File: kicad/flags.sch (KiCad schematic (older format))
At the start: 3 parts, among them U48 74LS173

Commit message: Update to current kicad libraries
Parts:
- removed D68, D69: LED, symbol LED
- removed U48: 74LS173, symbol 74LS173
- added D62, D63: LED, symbol Device:LED
- added U48: 74LS173, symbol 74xx:74LS173
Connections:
- net labels added: VCC
- wire segments 27 -> 26
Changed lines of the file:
@@
-EESchema Schematic File Version 2
-LIBS:power
-LIBS:device
-LIBS:transistors
-LIBS:conn
-LIBS:linear
-LIBS:regul
-LIBS:74xx
-LIBS:cmos4000
-LIBS:adc-dac
-LIBS:memory
-LIBS:xilinx
-LIBS:microcontrollers
-LIBS:dsp
-LIBS:microchip
-LIBS:analog_switches
-LIBS:motorola
-LIBS:texas
-LIBS:intel
-LIBS:audio
-LIBS:interface
-LIBS:digital-audio
-LIBS:philips
-LIBS:display
-LIBS:cypress
-LIBS:siliconi
-LIBS:opto
-LIBS:atmel
-LIBS:contrib
-LIBS:valves
-LIBS:switches
-LIBS:74xxx
-LIBS:28c16
-LIBS:sap-be-cache
-EELAYER 24 0
+EESchema Schematic File Version 4
+EELAYER 30 0
 EELAYER END
 $Descr A4 11693 8268
 encoding utf-8
-Sheet 12 12
+Sheet 12 13
 Title "Simple As Possible computer by Ben Eater"
 Date "2017-05-10"
@@
 Text HLabel 4650 1600 2    60   Output ~ 0
 ZF
-$Comp
-L 74LS173 U48
-U 1 1 5AD47646
-P 3600 2050
-F 0 "U48" H 3700 2150 50  0000 C CNN
-F 1 "74LS173" H 3700 2000 50  0000 C CNN
-F 2 "" H 3600 2050 50  0000 C CNN
-F 3 "" H 3600 2050 50  0000 C CNN
-	1    3600 2050
-	1    0    0    -1
-$EndComp
 Text Label 1550 950  2    60   ~ 0
 ~LOAD
-Text Label 2550 2300 0    60   ~ 0
+Text Label 2950 2400 0    60   ~ 0
 ~LOAD
-$Comp
-L GND #PWR090
-U 1 1 5AD4767C
-P 2450 2100
-F 0 "#PWR090" H 2450 1850 50  0001 C CNN
-F 1 "GND" H 2450 1950 50  0000 C CNN
-F 2 "" H 2450 2100 50  0000 C CNN
-F 3 "" H 2450 2100 50  0000 C CNN
-	1    2450 2100
-	1    0    0    -1
-$EndComp
-Text Label 2550 1500 0    60   ~ 0
+Text Label 2950 1500 0    60   ~ 0
 CARRY
-Text Label 2550 1600 0    60   ~ 0
+Text Label 2950 1600 0    60   ~ 0
 ZERO
 Text Label 1550 1450 2    60   ~ 0
@@
 Text Label 1550 1250 2    60   ~ 0
 RST
-Text Label 2600 2600 0    60   ~ 0
+Text Label 3000 2700 0    60   ~ 0
 RST
 Wire Wire Line
 	1550 950  1300 950
 Wire Wire Line
-	2550 2300 2800 2300
+	2950 2400 3200 2400
 Wire Wire Line
-	2800 2300 2900 2300
+	3200 2400 3300 2400
 Wire Wire Line
-	2800 2300 2800 2200
+	3200 2400 3200 2300
 Wire Wire Line
-	2800 2200 2900 2200
-Connection ~ 2800 2300
+	3200 2300 3300 2300
+Connection ~ 3200 2400
 Wire Wire Line
-	2900 2050 2800 2050
+	3300 2100 3200 2100
 Wire Wire Line
-	2800 2050 2450 2050
+	3300 2000 3200 2000
 Wire Wire Line
-	2450 2050 2450 2100
+	3200 2000 3200 2100
+Connection ~ 3200 2100
 Wire Wire Line
-	2900 1950 2800 1950
+	2950 1500 3300 1500
 Wire Wire Line
-	2800 1950 2800 2050
-Connection ~ 2800 2050
-Wire Wire Line
-	2550 1500 2900 1500
-Wire Wire Line
-	2550 1600 2900 1600
+	2950 1600 3300 1600
 Wire Wire Line
 	1550 1450 1300 1450
@@
 	1550 1100 1300 1100
 Wire Wire Line
-	2550 2600 2900 2600
+	2950 2700 3300 2700
 Wire Wire Line
-	2550 2400 2900 2400
-Text Label 2550 2400 0    60   ~ 0
+	2950 2500 3300 2500
+Text Label 2950 2500 0    60   ~ 0
 CLK
 Text Label 4450 1500 0    60   ~ 0
@@
 NoConn ~ 4300 1700
 NoConn ~ 4300 1800
-NoConn ~ 2900 1700
-NoConn ~ 2900 1800
-$Comp
-L LED D68
-U 1 1 5AD4AD3C
-P 5450 1800
-F 0 "D68" H 5450 1900 50  0000 C CNN
-F 1 "LED" H 5450 1700 50  0000 C CNN
-F 2 "" H 5450 1800 50  0000 C CNN
-F 3 "" H 5450 1800 50  0000 C CNN
-	1    5450 1800
-	0    -1   -1   0
-$EndComp
-$Comp
-L LED D69
-U 1 1 5AD4AD4E
-P 5750 1800
-F 0 "D69" H 5750 1900 50  0000 C CNN
-F 1 "LED" H 5750 1700 50  0000 C CNN
-F 2 "" H 5750 1800 50  0000 C CNN
-F 3 "" H 5750 1800 50  0000 C CNN
-	1    5750 1800
-	0    -1   -1   0
-$EndComp
-$Comp
-L GND #PWR091
-U 1 1 5AD4AD59
-P 5600 2100
-F 0 "#PWR091" H 5600 1850 50  0001 C CNN
-F 1 "GND" H 5600 1950 50  0000 C CNN
-F 2 "" H 5600 2100 50  0000 C CNN
-F 3 "" H 5600 2100 50  0000 C CNN
-	1    5600 2100
-	1    0    0    -1
-$EndComp
+NoConn ~ 3300 1700
+NoConn ~ 3300 1800
 Wire Wire Line
 	5600 2100 5600 2050
@@
 Text Label 5750 1600 1    60   ~ 0
 ZF
+$Comp
+L power:GND #PWR0156
+U 1 1 5EA8388C
+P 2800 2100
+F 0 "#PWR0156" H 2800 1850 50  0001 C CNN
+F 1 "GND" H 2805 1927 50  0000 C CNN
+F 2 "" H 2800 2100 50  0001 C CNN
+F 3 "" H 2800 2100 50  0001 C CNN
+	1    2800 2100
+	1    0    0    -1
+$EndComp
+Wire Wire Line
+	2800 2100 3200 2100
+$Comp
+L power:GND #PWR0159
+U 1 1 5EA8545C
+P 5600 2100
+F 0 "#PWR0159" H 5600 1850 50  0001 C CNN
+F 1 "GND" H 5605 1927 50  0000 C CNN
+F 2 "" H 5600 2100 50  0001 C CNN
+F 3 "" H 5600 2100 50  0001 C CNN
+	1    5600 2100
+	1    0    0    -1
+$EndComp
+$Comp
+L Device:LED D62
+U 1 1 5EA85B93
+P 5450 1800
+F 0 "D62" V 5489 1683 50  0000 R CNN
+F 1 "LED" V 5398 1683 50  0000 R CNN
+F 2 "" H 5450 1800 50  0001 C CNN
+F 3 "~" H 5450 1800 50  0001 C CNN
+	1    5450 1800
+	0    -1   -1   0
+$EndComp
+$Comp
+L Device:LED D63
+U 1 1 5EA8646D
+P 5750 1800
+F 0 "D63" V 5789 1683 50  0000 R CNN
+F 1 "LED" V 5698 1683 50  0000 R CNN
+F 2 "" H 5750 1800 50  0001 C CNN
+F 3 "~" H 5750 1800 50  0001 C CNN
+	1    5750 1800
+	0    -1   -1   0
+$EndComp
+$Comp
+L 74xx:74LS173 U48
+U 1 1 5EA87D23
+P 3800 2100
+F 0 "U48" H 3550 2850 50  0000 C CNN
+F 1 "74LS173" H 4000 1350 50  0000 C CNN
+F 2 "" H 3800 2100 50  0001 C CNN
+F 3 "http://www.ti.com/lit/gpn/sn74LS173" H 3800 2100 50  0001 C CNN
+	1    3800 2100
+	1    0    0    -1
+$EndComp
+$Comp
+L power:GND #PWR0158
+U 1 1 5EA8EB64
+P 3800 3000
+F 0 "#PWR0158" H 3800 2750 50  0001 C CNN
+F 1 "GND" H 3805 2827 50  0000 C CNN
+F 2 "" H 3800 3000 50  0001 C CNN
+F 3 "" H 3800 3000 50  0001 C CNN
+	1    3800 3000
+	1    0    0    -1
+$EndComp
+$Comp
+L power:VCC #PWR0157
+U 1 1 5EA8F117
+P 3800 1200
+F 0 "#PWR0157" H 3800 1050 50  0001 C CNN
+F 1 "VCC" H 3817 1373 50  0000 C CNN
+F 2 "" H 3800 1200 50  0001 C CNN
+F 3 "" H 3800 1200 50  0001 C CNN
+	1    3800 1200
+	1    0    0    -1
+$EndComp
 $EndSCHEMATC

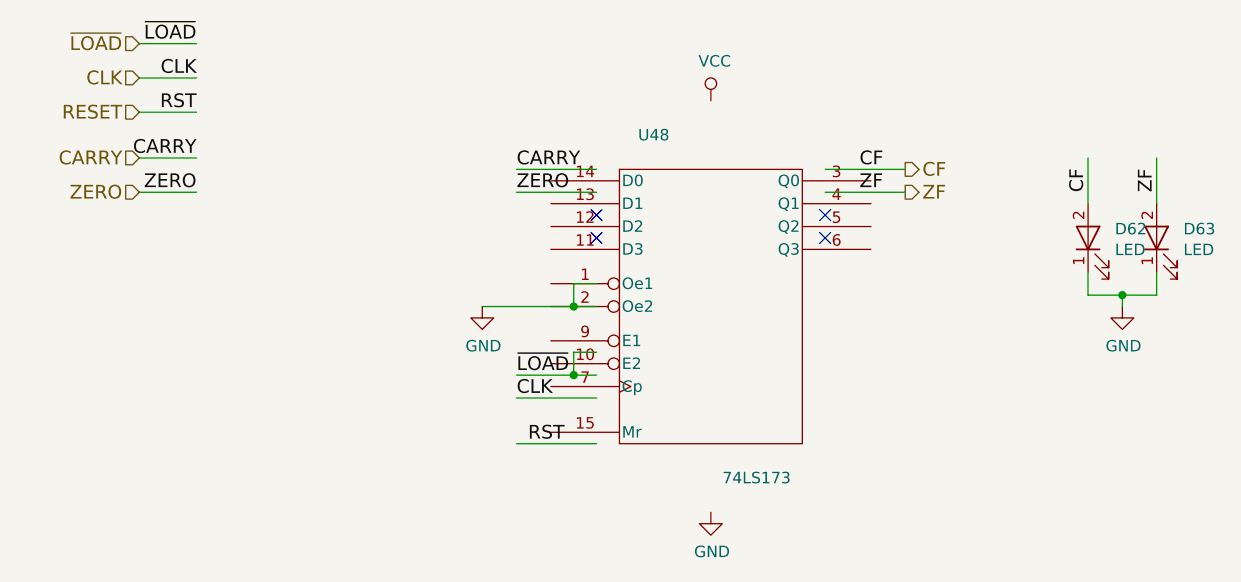
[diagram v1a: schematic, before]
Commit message: update bus names and improve sheet text
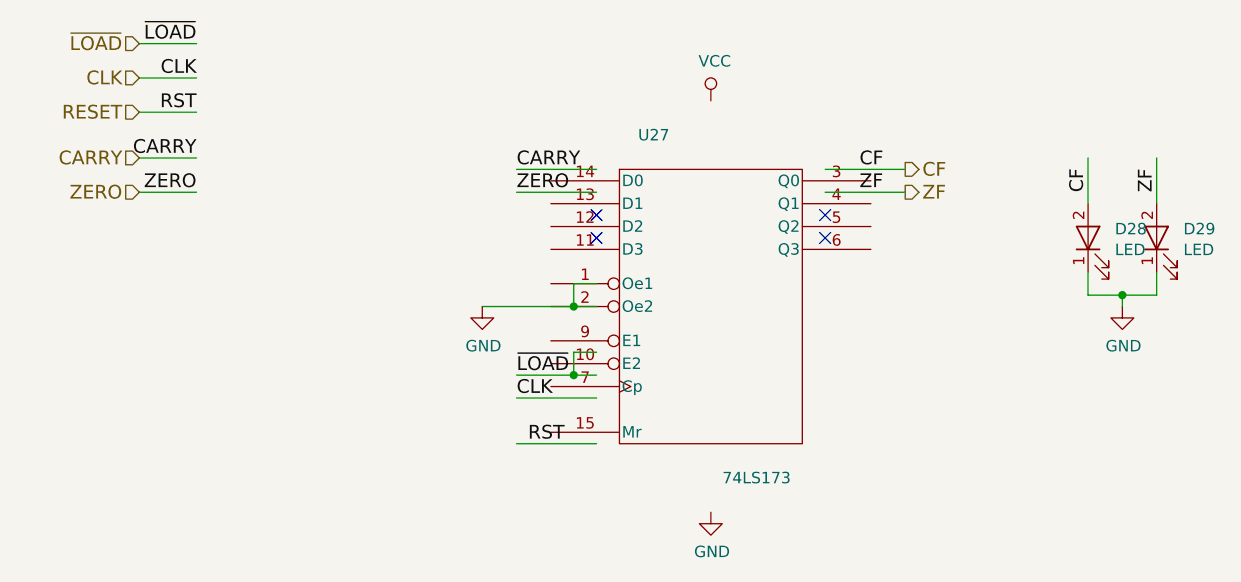
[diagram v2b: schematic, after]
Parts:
- renumbered D62 to D28, D63 to D29, U48 to U27
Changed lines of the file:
@@
 $Descr A4 11693 8268
 encoding utf-8
-Sheet 12 13
-Title "Simple As Possible computer by Ben Eater"
+Sheet 7 13
+Title "Simple As Possible computer"
 Date "2017-05-10"
 Rev "1"
 Comp "Schematic released as CC BY-SA"
-Comment1 "Schematic capture by Vincent Sanders"
+Comment1 "Schematic capture by Vincent Sanders of a design by Ben Eater"
 Comment2 "Flags register"
 Comment3 ""
@@
 ZF
 $Comp
-L power:GND #PWR0156
+L power:GND #PWR077
 U 1 1 5EA8388C
 P 2800 2100
-F 0 "#PWR0156" H 2800 1850 50  0001 C CNN
+F 0 "#PWR077" H 2800 1850 50  0001 C CNN
 F 1 "GND" H 2805 1927 50  0000 C CNN
 F 2 "" H 2800 2100 50  0001 C CNN
@@
 	2800 2100 3200 2100
 $Comp
-L power:GND #PWR0159
+L power:GND #PWR080
 U 1 1 5EA8545C
 P 5600 2100
-F 0 "#PWR0159" H 5600 1850 50  0001 C CNN
+F 0 "#PWR080" H 5600 1850 50  0001 C CNN
 F 1 "GND" H 5605 1927 50  0000 C CNN
 F 2 "" H 5600 2100 50  0001 C CNN
@@
 $EndComp
 $Comp
-L Device:LED D62
+L Device:LED D28
 U 1 1 5EA85B93
 P 5450 1800
-F 0 "D62" V 5489 1683 50  0000 R CNN
+F 0 "D28" V 5489 1683 50  0000 R CNN
 F 1 "LED" V 5398 1683 50  0000 R CNN
 F 2 "" H 5450 1800 50  0001 C CNN
@@
 $EndComp
 $Comp
-L Device:LED D63
+L Device:LED D29
 U 1 1 5EA8646D
 P 5750 1800
-F 0 "D63" V 5789 1683 50  0000 R CNN
+F 0 "D29" V 5789 1683 50  0000 R CNN
 F 1 "LED" V 5698 1683 50  0000 R CNN
 F 2 "" H 5750 1800 50  0001 C CNN
@@
 $EndComp
 $Comp
-L 74xx:74LS173 U48
+L 74xx:74LS173 U27
 U 1 1 5EA87D23
 P 3800 2100
-F 0 "U48" H 3550 2850 50  0000 C CNN
+F 0 "U27" H 3550 2850 50  0000 C CNN
 F 1 "74LS173" H 4000 1350 50  0000 C CNN
 F 2 "" H 3800 2100 50  0001 C CNN
@@
 $EndComp
 $Comp
-L power:GND #PWR0158
+L power:GND #PWR079
 U 1 1 5EA8EB64
 P 3800 3000
-F 0 "#PWR0158" H 3800 2750 50  0001 C CNN
+F 0 "#PWR079" H 3800 2750 50  0001 C CNN
 F 1 "GND" H 3805 2827 50  0000 C CNN
 F 2 "" H 3800 3000 50  0001 C CNN
@@
 $EndComp
 $Comp
-L power:VCC #PWR0157
+L power:VCC #PWR078
 U 1 1 5EA8F117
 P 3800 1200
-F 0 "#PWR0157" H 3800 1050 50  0001 C CNN
+F 0 "#PWR078" H 3800 1050 50  0001 C CNN
 F 1 "VCC" H 3817 1373 50  0000 C CNN
 F 2 "" H 3800 1200 50  0001 C CNN
